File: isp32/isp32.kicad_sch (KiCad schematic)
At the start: 98 parts, among them J1 BAT1, J10 LoRa_ANT, J12 Micro_SD_Card, J2 Switching, J3 USB_C_Receptacle_USB2.0, J4 ESP_JTAG, J5 GPS_ANT, J6 F0, J7 F1, J9 ANT, M1 Motor_Servo, M2 Motor_Servo, M3 Motor_Servo, M4 Motor_Servo, Q1 BSS138, Q2 BSS138, Q3 IRLML6402, Q4 BSS138, Q5 IRLML6402, Q6 S8050, SW1 RST, SW2 IO0, U1 SC189ZSKTRT, U10 BMP280, U11 MPU-9250, U2 USBLC6-2SC6, U3 STM32F030F4Px, U4 MP1660GTF-Z, U6 24LC32, U7 NEO-XM, U8 ESP32-S3-WROOM-1U, U9 RFM98W-315S2

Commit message: Replace F0 to G0
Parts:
- removed U3: STM32F030F4Px, Package_SO:TSSOP-20_4.4x6.5mm_P0.65mm, symbol MCU_ST_STM32F0:STM32F030F4Px
- added U3: STM32G030F6, Package_SO:TSSOP-20_4.4x6.5mm_P0.65mm, symbol STM32G030F6:STM32G030F6
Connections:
- net +3V3: now also U3.4 (VDD)
- net Buzz: now also U3.7 (PA0); no longer U8.39 (IO1)
- net GND: now also U3.5 (VSS)
- net RGB: now also U3.8 (PA1)
- net RST: now also U3.6 (NRST)
- net SCL: now also U3.1 (PB7/PB8)
- net SDA: now also U3.2 (PB9/PC14-OSC32_IN)
- net SERVO0: now also U3.11 (PA4)
- net SERVO1: now also U3.12 (PA5)
- net SERVO2: now also U3.13 (PA6)
- net SERVO3: now also U3.14 (PA7)
- net SWCLK: now also U3.19 (PA15/PA14-BOOT0)
- net SWDIO: now also U3.18 (PA13)
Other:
- moved on the sheet: C3

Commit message: Fix all isp32 issues
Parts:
- removed D1: GPS_LED, LED_SMD:LED_0603_1608Metric, symbol Device:LED_Small
- removed D3: WS2812, LED_SMD:LED_WS2812_PLCC6_5.0x5.0mm_P1.6mm, symbol LED:WS2812
- removed H1, H2, H3, H4: MountingHole, MountingHole:MountingHole_3.2mm_M3_ISO7380, symbol Mechanical:MountingHole
- removed J4: ESP_JTAG, Connector_PinHeader_1.27mm:PinHeader_1x06_P1.27mm_Vertical, symbol Connector_Generic:Conn_01x06
- removed L1: 1u, Inductor_SMD:L_Bourns-SRN4018, symbol Device:L_Small
- removed Q2: BSS138, Package_TO_SOT_SMD:SOT-23, symbol Transistor_FET:BSS138
- removed Q6: S8050, Package_TO_SOT_SMD:SOT-23, symbol Transistor_BJT:S8050
- removed R13: 330, Resistor_SMD:R_0603_1608Metric, symbol Device:R_Small
- removed SW2: IO0, Button_Switch_SMD:SW_SPST_B3U-1000P, symbol Switch:SW_Push
- removed TP2: TP5v, TestPoint:TestPoint_Pad_D1.0mm, symbol Connector:TestPoint
- removed TP6: 3V3, TestPoint:TestPoint_Pad_D1.0mm, symbol Connector:TestPoint
- removed TP7: SWDIO, TestPoint:TestPoint_Pad_D1.0mm, symbol Connector:TestPoint
- removed TP8: SWCLK, TestPoint:TestPoint_Pad_D1.0mm, symbol Connector:TestPoint
- removed TP9: GND, TestPoint:TestPoint_Pad_D1.0mm, symbol Connector:TestPoint
- removed U1: SC189ZSKTRT, Package_TO_SOT_SMD:SOT-23-5, symbol SC189ZSKTRT:SC189ZSKTRT
- removed U2: USBLC6-2SC6, Package_TO_SOT_SMD:SOT-23-6, symbol Power_Protection:USBLC6-2SC6
- removed U4: MP1660GTF-Z, Package_TO_SOT_SMD:SOT-563, symbol MP1660GTF-Z:MP1660GTF-Z
- added C12: 220u, Capacitor_Tantalum_SMD:CP_EIA-3528-12_Kemet-T, symbol Device:C_Small
- added C15: 10u, Capacitor_SMD:C_0805_2012Metric, symbol Device:C_Small
- added D1: Zener, Diode_SMD:D_SOD-123, symbol Device:D_Zener_Small
- added D3: ESP_LED, LED_SMD:LED_0603_1608Metric, symbol Device:LED_Small
- added D6: TVS, Diode_SMD:D_SMB, symbol Device:D_TVS_Filled
- added D7: WS2812B, LED_SMD:LED_WS2812B_PLCC4_5.0x5.0mm_P3.2mm, symbol LED:WS2812B
- added H1, H2, H3, H4: MountingHole_Pad, MountingHole:MountingHole_3.2mm_M3_ISO7380_Pad, symbol Mechanical:MountingHole_Pad
- added J4: ADC, Connector_PinHeader_1.27mm:PinHeader_1x05_P1.27mm_Vertical, symbol Connector_Generic:Conn_01x05
- added J8: BUZZ, Connector_PinHeader_1.27mm:PinHeader_1x02_P1.27mm_Vertical, symbol Connector_Generic:Conn_01x02
- added Q2: S8050, Package_TO_SOT_SMD:SOT-23, symbol Device:Q_NPN_BCE
- added Q6, Q7: IRLML6402, Package_TO_SOT_SMD:SOT-23, symbol Transistor_FET:IRLML6402
- added R26, R27: 100k, Resistor_SMD:R_0603_1608Metric, symbol Device:R_Small
- added U1: AZ1117-3.3, Package_TO_SOT_SMD:SOT-89-3, symbol Regulator_Linear:AZ1117-3.3
- added U2: MP2315, Package_TO_SOT_SMD:TSOT-23-8, symbol MP2315:MP2315
- C10: value 220u -> 22u; footprint Capacitor_Tantalum_SMD:CP_EIA-3528-12_Kemet-T -> Capacitor_SMD:C_0603_1608Metric
- C4: value 1u -> 100n
- C5: value 10u -> 100n
- C6: footprint Capacitor_SMD:C_0805_2012Metric -> Capacitor_SMD:C_0603_1608Metric
- C7: value 10p -> NC
- L2: value 22u -> NC
- L3: value 4.7u -> 5.5
- R10: value 5.49k -> 7k5
- R12: value 22 -> NC
- R19: value 100K -> 1k
- R21: value 100K -> 75k
- R8: value 10 -> 20
- R9: value 18k -> 20k
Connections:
- net UD+ is gone; now on net D+: J3.A6 (D+), J3.B6 (D+)
- net UD- is gone; now on net D-: J3.A7 (D-), J3.B7 (D-)
- net +3V3: now also C12.1, U1.2 (VO); no longer C6.1, R19.1
- net +5V: now also C6.1, D7.1 (VDD), J8.1 (Pin_1), Q7.2 (S), U1.3 (VI); no longer C1.1, C2.1, C7.2, C8.1, L3.2, R11.2, R21.1
- net +BATT: now also C15.1, D1.1 (K), Q6.2 (S), U2.2 (IN), U2.7 (VCC); no longer J1.1 (Pin_1)
- net Buzz: now also U3.3 (PC15-OSC32_OUT), Q2.1 (B); no longer U3.7 (PA0)
- net GND: now also J1.1 (Pin_1), R21.2, C12.2, C15.2, D3.1 (K), D6.1 (A1), D7.3 (VSS), H1.1, H2.1, H3.1, H4.1, J4.5 (Pin_5), Q2.3 (E), R26.2, R27.2, U1.1 (GND), U2.4 (GND); no longer J1.2 (Pin_2)
- net IMU_SS: no longer U11.22 (~{CS}), U8.6 (IO6)
- net IO0: no longer U8.27 (IO0)
- net RGB: now also U3.17 (PA12[PA10]), D7.4 (DIN); no longer R19.2, U3.8 (PA1)
- net SCL: now also U11.23 (SCL/SCLK)
- net SDA: now also U11.24 (SDA/MOSI)
- net at R3.2: now also U2.6 (EN)
- net LORA_BUSY: now reaches U9.16 (DIO2)
- net LORA_BUSY: now also U8.31 (IO38)
- net at C4.2, L3.1: now also U2.3 (SW)
- net INDI: now reaches U8.39 (IO1)
- net INDI: now also R19.1
- net at R8.1: now also U2.5 (BST)
- net at R9.1: now also U2.8 (FB)
- net at LS1.N: now also J8.2 (Pin_2), Q2.2 (C)
- net ADC3: now reaches U3.10 (PA3)
- net ADC3: now also J4.4 (Pin_4)
- net ADC2: now reaches U3.9 (PA2)
- net ADC2: now also J4.3 (Pin_3)
- net LORA_INT: no longer names the net of U9.14 (DIO0)
- net LORA_INT: no longer U8.31 (IO38)
- net MISO renamed MISO_1
- net MISO_1: no longer J12.7 (DAT0), U11.9 (AD0/MISO)
- net MOSI renamed MOSI_1
- net MOSI_1: no longer J12.3 (CMD), U11.24 (SDA/MOSI)
- net RX: no longer names the net of U8.37 (TXD0)
- net SCK renamed SCK_1
- net SCK_1: no longer J12.5 (CLK), U11.23 (SCL/SCLK)
- net TCK renamed MOSI_2
- net MOSI_2: now also J12.3 (CMD)
- net TDI renamed MISO_2
- net MISO_2: now also J12.7 (DAT0)
- net TDO renamed SCK_2
- net SCK_2: now also J12.5 (CLK)
- net TMS: no longer names the net of U8.35 (IO42)
- net TX: no longer names the net of U8.36 (RXD0)
- new net: Q7.1 (G), R27.1
- new net: C1.1, C2.1, C7.2, C8.1, L3.2, Q7.3 (D), R11.2
- new net: D1.2 (A), Q6.1 (G), R26.1
- new net: D3.2 (A), R19.2
- new net: D6.2 (A2), J1.2 (Pin_2), Q6.3 (D)
- new net: R21.1, U2.1 (AAM)
- new net ADC0: J4.1 (Pin_1), U3.7 (PA0)
- new net ADC1: J4.2 (Pin_2), U3.8 (PA1)
- no-connect marks 36 -> 40
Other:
- note added: "Out Port"
- note removed: "Debug Port"
- moved on the sheet: C1, C2, C4, C5, C7, C8, D5, J1, J5, L3, LS1, R10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

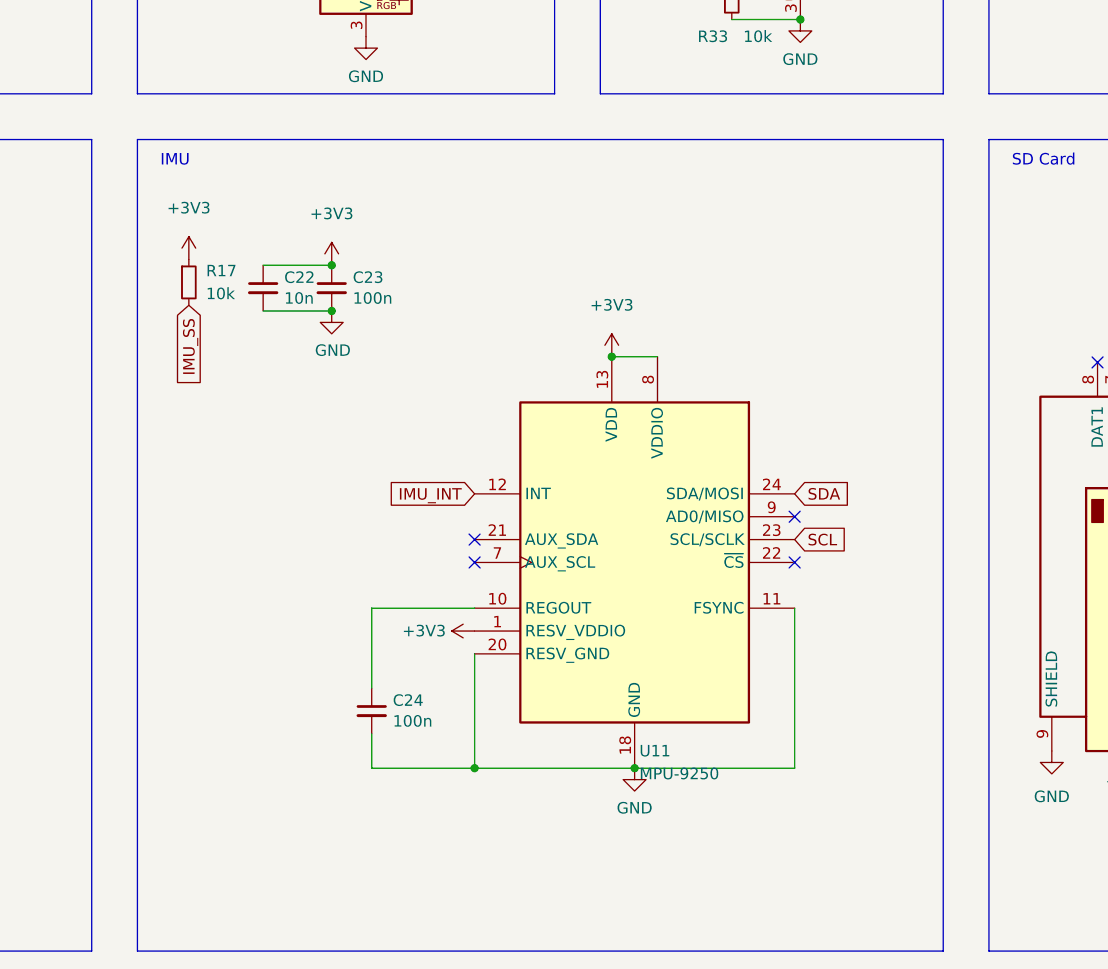
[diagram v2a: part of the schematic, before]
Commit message: feat: add level converter to imu
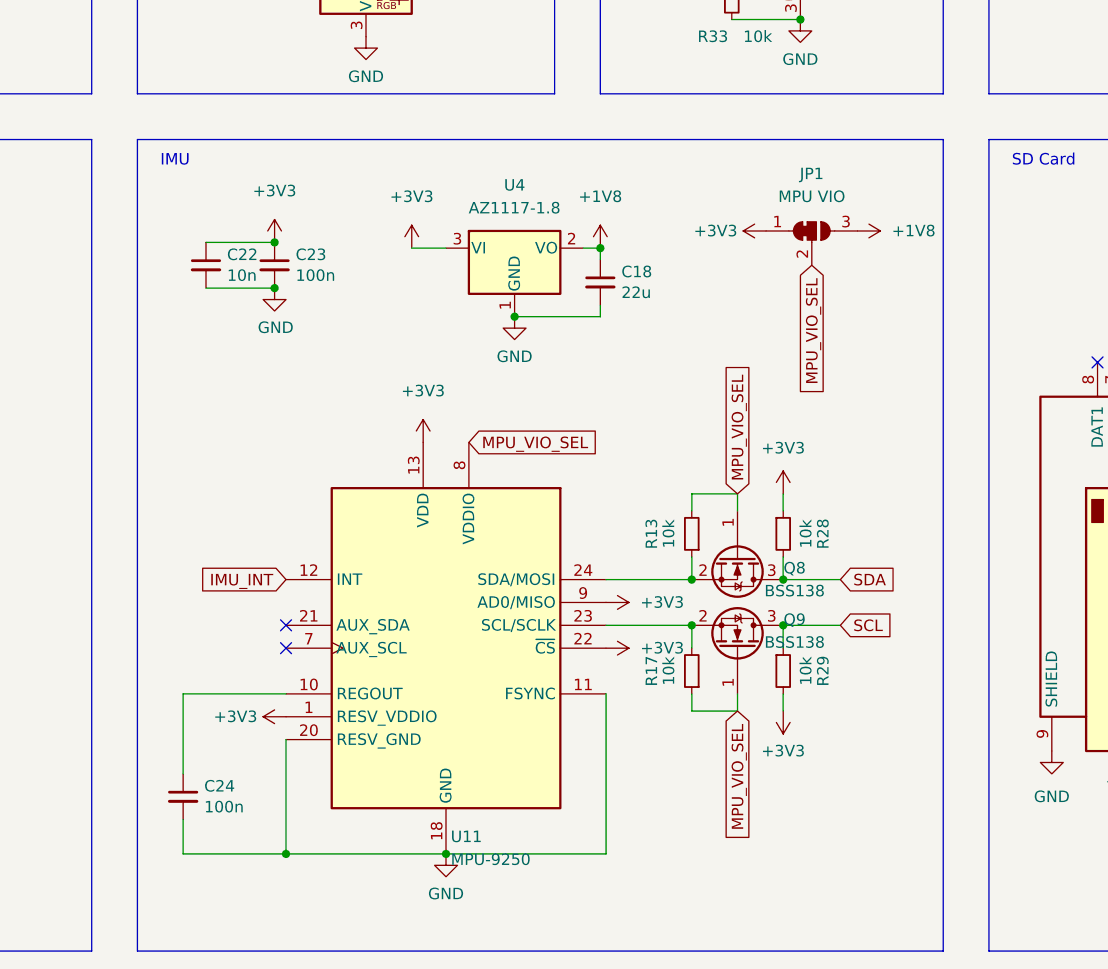
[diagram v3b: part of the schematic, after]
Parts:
- added C18: 22u, Capacitor_SMD:C_0603_1608Metric, symbol Device:C_Small
- added JP1: MPU VIO, symbol Jumper:SolderJumper_3_Bridged12
- added Q8, Q9: BSS138, Package_TO_SOT_SMD:SOT-23, symbol Transistor_FET:BSS138
- added R13, R28, R29: 10k, Resistor_SMD:R_0603_1608Metric, symbol Device:R_Small
- added U4: AZ1117-1.8, Package_TO_SOT_SMD:SOT-89-3, symbol Regulator_Linear:AZ1117-1.8
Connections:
- net +3V3: now also U11.22 (~{CS}), U11.9 (AD0/MISO), JP1.1 (A), R28.1, R29.2, U4.3 (VI); no longer R17.1, U11.8 (VDDIO)
- net GND: now also C18.2, U4.1 (GND)
- net SCL: now also Q9.3 (D), R29.1; no longer U11.23 (SCL/SCLK)
- net SDA: now also Q8.3 (D), R28.2; no longer U11.24 (SDA/MOSI)
- net IMU_SS: no longer names the net of R17.2
- net IMU_SS: now also U11.23 (SCL/SCLK), Q9.2 (S)
- new net: Q8.2 (S), R13.1, U11.24 (SDA/MOSI)
- new net +1V8: C18.1, JP1.3 (B), U4.2 (VO)
- new net MPU_VIO_SEL: JP1.2 (C), Q8.1 (G), Q9.1 (G), R13.2, R17.1, U11.8 (VDDIO)
- no-connect marks 40 -> 38
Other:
- moved on the sheet: C22, C23, C24, U11

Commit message: feat: isp32 2023 12 19
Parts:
- removed Q7: IRLML6402, Package_TO_SOT_SMD:SOT-23, symbol Transistor_FET:IRLML6402
- removed R27: 100k, Resistor_SMD:R_0603_1608Metric, symbol Device:R_Small
- added D8: D_Shockley, Diode_SMD:D_SOD-123, symbol Device:D_Shockley
- added J11: Power Modules, Connector_PinSocket_2.54mm:PinSocket_1x04_P2.54mm_Vertical, symbol Connector_Generic:Conn_01x04
- JP1: footprint (none) -> Jumper:SolderJumper-3_P1.3mm_Bridged12_RoundedPad1.0x1.5mm_NumberLabels
- L2: value NC -> 22u
- R12: value NC -> 22
- U1: footprint Package_TO_SOT_SMD:SOT-89-3 -> Package_TO_SOT_SMD:SOT-223-3_TabPin2
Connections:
- net +5V: now also D8.1 (K)
- net +BATT: now also J11.1 (Pin_1), J11.2 (Pin_2)
- net GND: now also J11.3 (Pin_3)
- net IO0: now also U8.27 (IO0)
- net RST: no longer U3.6 (NRST)
- net at C1.1, C2.1, C7.2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: now also D8.2 (A), J11.4 (Pin_4)
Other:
- moved on the sheet: C10, C12, C6, U1
